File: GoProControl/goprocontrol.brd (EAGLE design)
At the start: 54.2 x 51.8 mm, 17 parts, among them Q1 IRLML6344

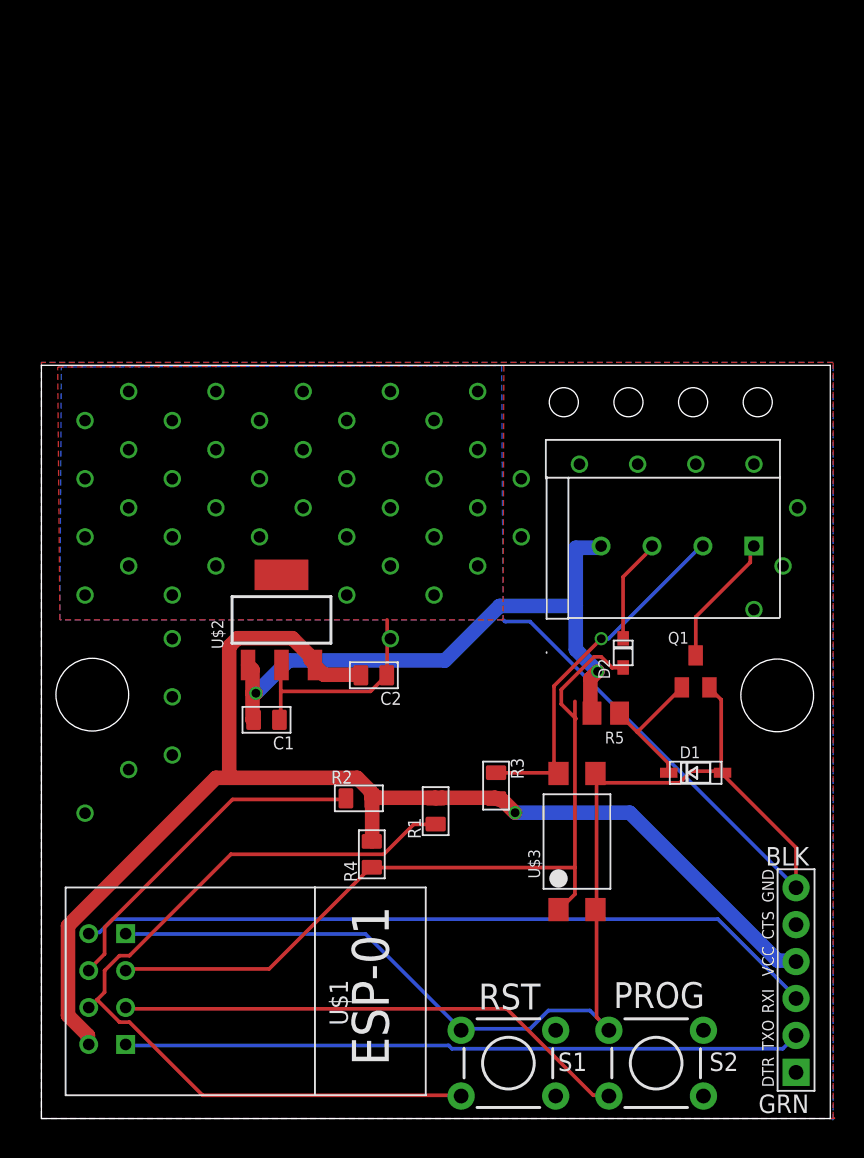
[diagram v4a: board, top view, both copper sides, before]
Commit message: v0.3
- heat sink vias are now 0.35mm and have no exposed copper
- 2x the number of heat sink vias
- improved labels
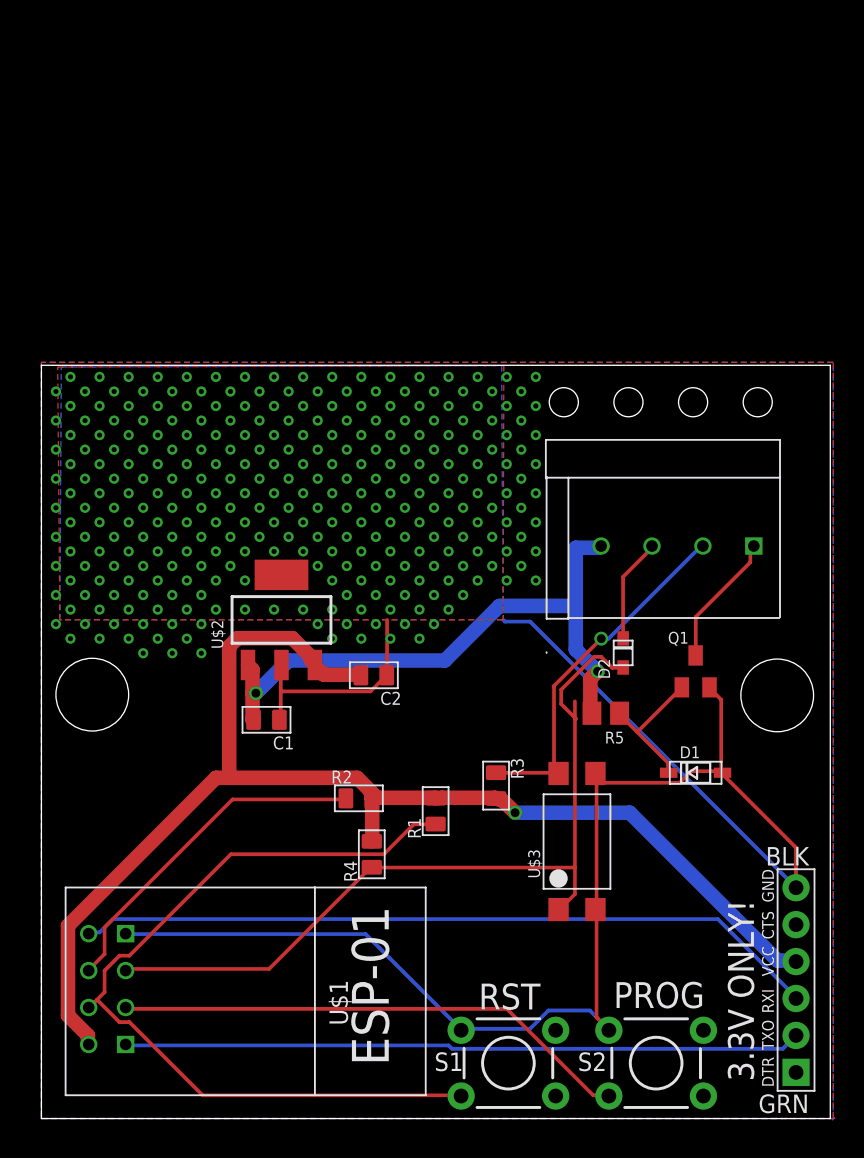
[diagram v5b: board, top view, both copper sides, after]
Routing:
- net GND: vias 53 -> 299
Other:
- board text added: "3.3V ONLY!"
- board text added: "GoProControl v0.3 http://synfin.net/goprocontrol"
- board text removed: "GoProControl v0.2 http://synfin.net/goprocontrol"

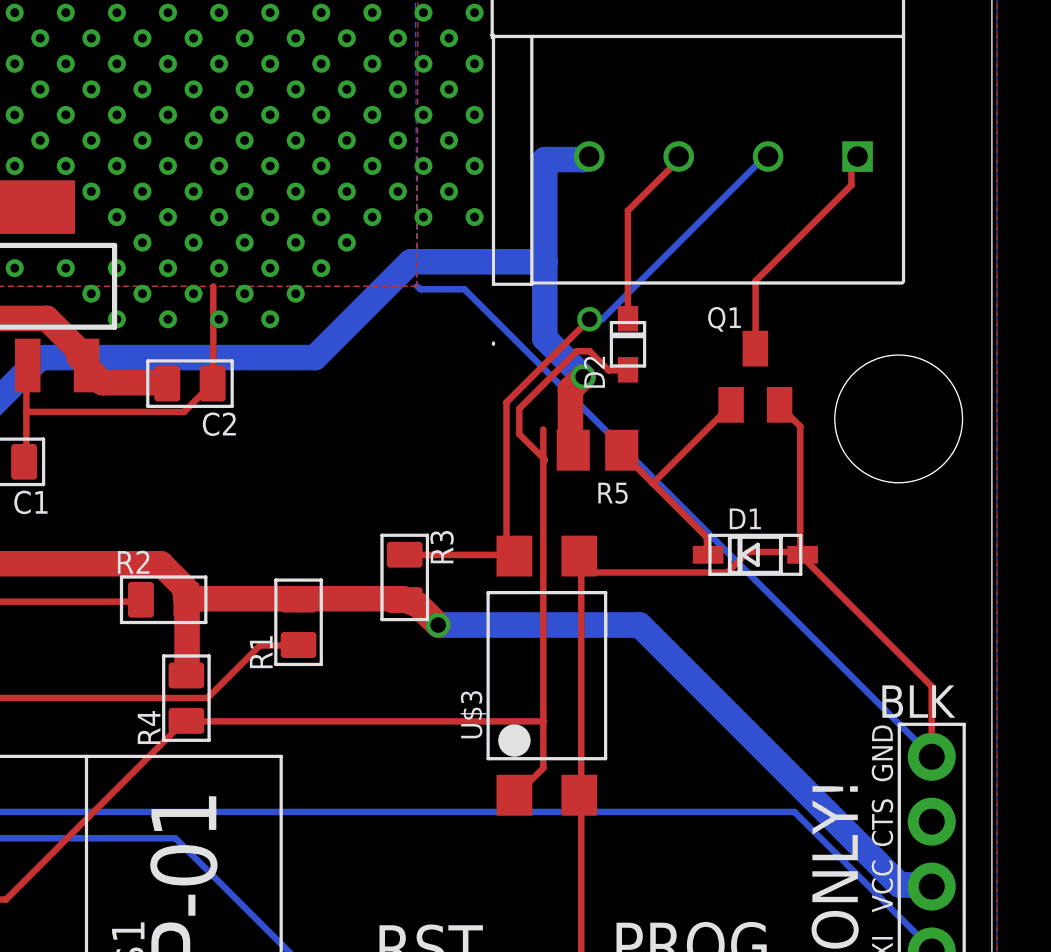
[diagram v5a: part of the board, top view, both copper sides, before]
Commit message: v0.4 fix diode pads
My old sod-323 and sod-123 pads always seemed a bit wrong/too small
these new pads are better.
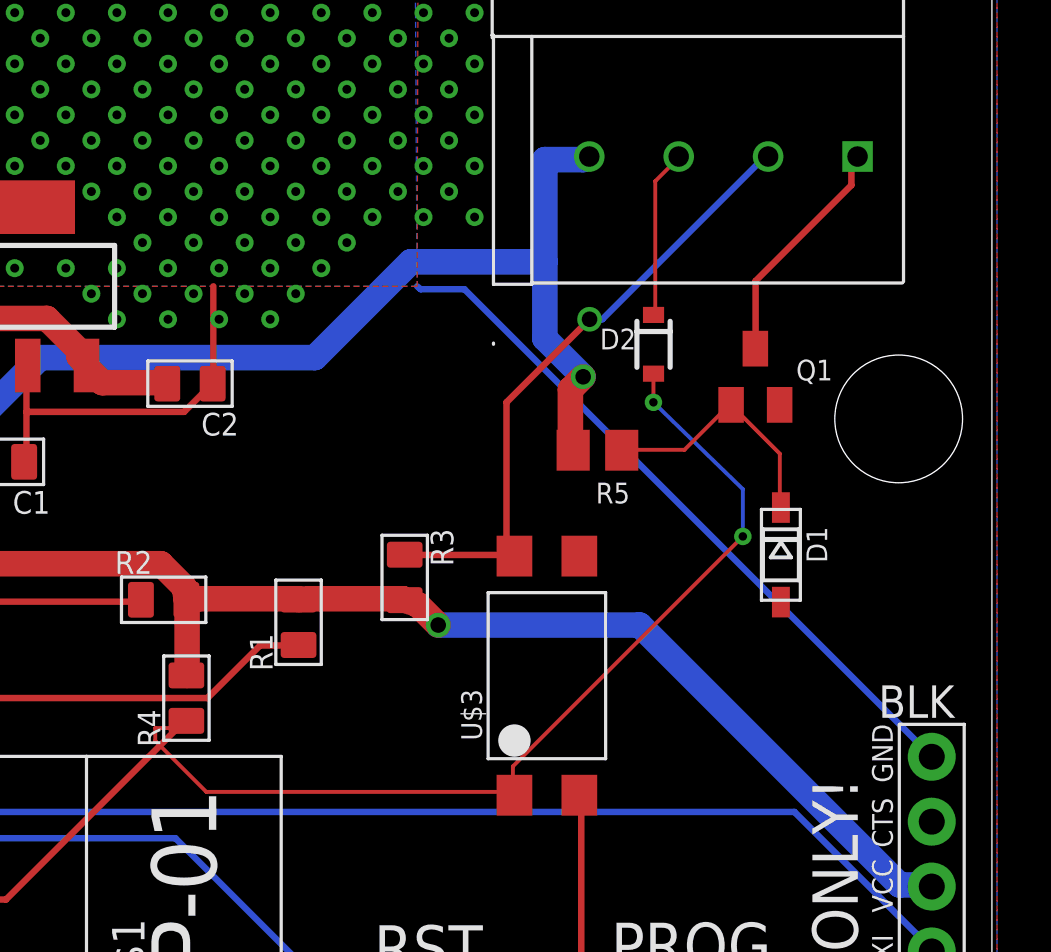
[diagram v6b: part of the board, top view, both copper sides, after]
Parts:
- D2: device synfinatic:SOD-323F -> synfinatic:SOD-323
- moved D1 1.00 mm to (46.0, 23.8), turned to 270 degrees
- moved D2 1.00 mm to (41.0, 32.0), turned to 270 degrees
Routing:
- net GND: track 124.3 -> 89.0 mm
- net GPIO2: track 56.7 -> 58.6 mm, vias 0 -> 2
- net INPUT: track 7.22 -> 6.61 mm
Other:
- board text added: "GoProControl v0.4 http://synfin.net/goprocontrol"
- board text removed: "GoProControl v0.3 http://synfin.net/goprocontrol"
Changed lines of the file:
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@@
 <grid distance="1" unitdist="mm" unit="mm" style="lines" multiple="1" display="no" altdistance="0.05" altunitdist="mm" altunit="mm"/>
 <layers>
-<layer number="1" name="Top" color="4" fill="1" visible="yes" active="yes"/>
-<layer number="16" name="Bottom" color="1" fill="1" visible="yes" active="yes"/>
+<layer number="1" name="Top" color="4" fill="1" visible="no" active="yes"/>
+<layer number="16" name="Bottom" color="1" fill="1" visible="no" active="yes"/>
 <layer number="17" name="Pads" color="2" fill="1" visible="yes" active="yes"/>
 <layer number="18" name="Vias" color="2" fill="1" visible="yes" active="yes"/>
@@
 <hole x="3.5" y="29.15" drill="5"/>
 <hole x="50.6" y="29.1" drill="5"/>
-<text x="48" y="16" size="1.016" layer="26" rot="MR0">GoProControl v0.3
+<text x="48" y="16" size="1.016" layer="26" rot="MR0">GoProControl v0.4
 http://synfin.net/goprocontrol</text>
 <text x="48" y="11.5" size="1.778" layer="26" rot="MR0">S/N:</text>
@@
 <attribute name="NAME" x="24.765" y="29.337" size="0.889" layer="25" font="vector" ratio="11" rot="R180"/>
 </element>
-<element name="D1" library="adafruit" package="SOD-123" value="10V Z" x="44.99" y="23.78" smashed="yes">
-<attribute name="NAME" x="43.89" y="24.78" size="0.8128" layer="25"/>
-</element>
-<element name="D2" library="synfinatic" package="SOD-323F" value="B5817WS" x="40.005" y="32.02" smashed="yes" rot="R90">
-<attribute name="NAME" x="39.105" y="30.22" size="0.8128" layer="25" font="vector" rot="R90"/>
+<element name="D1" library="adafruit" package="SOD-123" value="10V Z" x="45.99" y="23.78" smashed="yes" rot="R270">
+<attribute name="NAME" x="46.99" y="24.88" size="0.8128" layer="25" rot="R270"/>
+</element>
+<element name="D2" library="synfinatic" package="SOD-323" value="B5817WS" x="41.005" y="32.02" smashed="yes" rot="R270">
+<attribute name="NAME" x="38.905" y="31.82" size="0.8128" layer="25" font="vector"/>
 </element>
 <element name="JP1" library="SparkFun-Connectors" package="FTDI_DEVICE_SIDE" value="FTDI_DEVICE" x="51.895" y="9.525" rot="R90"/>
 <element name="Q1" library="synfinatic" package="SOT23" value="IRLML6344" x="44.99" y="30.75" smashed="yes">
-<attribute name="NAME" x="43.085" y="32.655" size="0.8128" layer="25"/>
+<attribute name="NAME" x="46.585" y="30.605" size="0.8128" layer="25"/>
 </element>
 <element name="R1" library="Seeed-OPL-Resistor" package="R0805" value="1K" x="27.11" y="21.14" smashed="yes" rot="R180">
@@
 <wire x1="16.4592" y1="29.3751" x2="22.6314" y2="29.3751" width="0.254" layer="1"/>
 <wire x1="23.6601" y1="30.4038" x2="23.749" y2="30.48" width="0.254" layer="1"/>
-<wire x1="46.7487" y1="28.8036" x2="46.7487" y2="23.8887" width="0.254" layer="1"/>
-<wire x1="45.9486" y1="29.6037" x2="46.7487" y2="28.8036" width="0.254" layer="1"/>
-<wire x1="46.7487" y1="23.8887" x2="46.84" y2="23.78" width="0.254" layer="1"/>
-<wire x1="45.9486" y1="29.6037" x2="45.94" y2="29.65" width="0.254" layer="1"/>
 <wire x1="38.1762" y1="6.9723" x2="38.1762" y2="14.2875" width="0.254" layer="1"/>
 <wire x1="38.9763" y1="6.1722" x2="38.1762" y2="6.9723" width="0.254" layer="1"/>
 <wire x1="38.1762" y1="14.2875" x2="38.1" y2="14.37" width="0.254" layer="1"/>
 <wire x1="38.9763" y1="6.1722" x2="39.0238" y2="6.0706" width="0.254" layer="1"/>
-<wire x1="38.1762" y1="14.4018" x2="38.1762" y2="23.6601" width="0.254" layer="1"/>
-<wire x1="38.1762" y1="23.6601" x2="38.1" y2="23.73" width="0.254" layer="1"/>
-<wire x1="38.1762" y1="14.4018" x2="38.1" y2="14.37" width="0.254" layer="1"/>
-<wire x1="44.6913" y1="23.8887" x2="46.6344" y2="23.8887" width="0.254" layer="1"/>
-<wire x1="43.8912" y1="23.0886" x2="44.6913" y2="23.8887" width="0.254" layer="1"/>
-<wire x1="38.2905" y1="23.0886" x2="43.8912" y2="23.0886" width="0.254" layer="1"/>
-<wire x1="46.6344" y1="23.8887" x2="46.84" y2="23.78" width="0.254" layer="1"/>
-<wire x1="38.2905" y1="23.0886" x2="38.1" y2="23.73" width="0.254" layer="1"/>
-<wire x1="51.8922" y1="18.6309" x2="51.8922" y2="15.8877" width="0.254" layer="1"/>
-<wire x1="46.863" y1="23.6601" x2="51.8922" y2="18.6309" width="0.254" layer="1"/>
-<wire x1="51.8922" y1="15.8877" x2="51.895" y2="15.875" width="0.254" layer="1"/>
-<wire x1="46.863" y1="23.6601" x2="46.84" y2="23.78" width="0.254" layer="1"/>
 <wire x1="33.6042" y1="34.1757" x2="31.8897" y2="34.1757" width="0.254" layer="16"/>
 <wire x1="51.8922" y1="15.8877" x2="33.6042" y2="34.1757" width="0.254" layer="16"/>
@@
 <contactref element="R5" pad="1"/>
 <contactref element="D1" pad="C"/>
-<wire x1="43.0911" y1="24.4602" x2="43.0911" y2="23.8887" width="0.254" layer="1"/>
-<wire x1="39.7764" y1="27.7749" x2="40.97655" y2="26.57475" width="0.254" layer="1"/>
-<wire x1="40.97655" y1="26.57475" x2="43.0911" y2="24.4602" width="0.254" layer="1"/>
-<wire x1="43.0911" y1="23.8887" x2="43.14" y2="23.78" width="0.254" layer="1"/>
-<wire x1="39.7764" y1="27.7749" x2="39.76" y2="27.875" width="0.254" layer="1"/>
-<wire x1="40.97655" y1="26.57475" x2="44.0055" y2="29.6037" width="0.254" layer="1"/>
-<wire x1="44.0055" y1="29.6037" x2="44.04" y2="29.65" width="0.254" layer="1"/>
+<wire x1="45.9486" y1="27.7368" x2="45.9486" y2="25.6794" width="0.1524" layer="1"/>
+<wire x1="44.0436" y1="29.6418" x2="45.9486" y2="27.7368" width="0.1524" layer="1"/>
+<wire x1="45.9486" y1="25.6794" x2="45.99" y2="25.63" width="0.1524" layer="1"/>
+<wire x1="44.0436" y1="29.6418" x2="44.04" y2="29.65" width="0.1524" layer="1"/>
+<wire x1="42.2148" y1="27.8892" x2="39.7764" y2="27.8892" width="0.1524" layer="1"/>
+<wire x1="43.9674" y1="29.6418" x2="42.2148" y2="27.8892" width="0.1524" layer="1"/>
+<wire x1="39.7764" y1="27.8892" x2="39.76" y2="27.875" width="0.1524" layer="1"/>
+<wire x1="43.9674" y1="29.6418" x2="44.04" y2="29.65" width="0.1524" layer="1"/>
 </signal>
 <signal name="GND_MAIN">
@@
 <contactref element="R4" pad="1"/>
 <contactref element="U$3" pad="1"/>
-<wire x1="36.6903" y1="15.4305" x2="36.6903" y2="17.2593" width="0.254" layer="1"/>
-<wire x1="36.6903" y1="17.2593" x2="36.6903" y2="27.5" width="0.254" layer="1"/>
-<wire x1="36.6903" y1="27.5" x2="36.6903" y2="28.6893" width="0.254" layer="1"/>
-<wire x1="35.6616" y1="14.4018" x2="36.6903" y2="15.4305" width="0.254" layer="1"/>
-<wire x1="35.6616" y1="14.4018" x2="35.56" y2="14.37" width="0.254" layer="1"/>
-<wire x1="36.6903" y1="17.2593" x2="22.7457" y2="17.2593" width="0.254" layer="1"/>
-<wire x1="22.7457" y1="17.2593" x2="22.72" y2="17.281" width="0.254" layer="1"/>
 <wire x1="15.6591" y1="10.287" x2="5.8293" y2="10.287" width="0.254" layer="1"/>
 <wire x1="22.6314" y1="17.2593" x2="15.6591" y2="10.287" width="0.254" layer="1"/>
 <wire x1="5.8293" y1="10.287" x2="5.7925" y2="10.175" width="0.254" layer="1"/>
 <wire x1="22.6314" y1="17.2593" x2="22.72" y2="17.281" width="0.254" layer="1"/>
-<wire x1="39.25" y1="31" x2="40" y2="31" width="0.254" layer="1"/>
-<wire x1="38.5" y1="31.75" x2="39.25" y2="31" width="0.254" layer="1"/>
-<wire x1="38" y1="31.75" x2="38.5" y2="31.75" width="0.254" layer="1"/>
-<wire x1="35.75" y1="29.5" x2="38" y2="31.75" width="0.254" layer="1"/>
-<wire x1="35.75" y1="28.5" x2="35.75" y2="29.5" width="0.254" layer="1"/>
-<wire x1="36.75" y1="27.5" x2="35.75" y2="28.5" width="0.254" layer="1"/>
-<wire x1="40" y1="31" x2="40.005" y2="31.02" width="0.254" layer="1"/>
-<wire x1="36.75" y1="27.5" x2="36.6903" y2="27.5" width="0.254" layer="1"/>
+<wire x1="41" y1="29.75" x2="41" y2="31" width="0.1524" layer="1"/>
+<wire x1="44.5" y1="26.35" x2="41" y2="29.75" width="0.1524" layer="16"/>
+<wire x1="44.5" y1="24.5" x2="44.5" y2="26.35" width="0.1524" layer="16"/>
+<wire x1="35.5" y1="15.5" x2="44.5" y2="24.5" width="0.1524" layer="1"/>
+<wire x1="35.5" y1="14.5" x2="35.5" y2="15.5" width="0.1524" layer="1"/>
+<wire x1="41" y1="31" x2="41.005" y2="30.87" width="0.1524" layer="1"/>
+<wire x1="23.5" y1="14.5" x2="35.5" y2="14.5" width="0.1524" layer="1"/>
+<wire x1="21.5" y1="16.5" x2="23.5" y2="14.5" width="0.1524" layer="1"/>
+<wire x1="21.5" y1="17" x2="21.5" y2="16.5" width="0.1524" layer="1"/>
+<wire x1="22.5" y1="17" x2="21.5" y2="17" width="0.1524" layer="1"/>
+<wire x1="35.5" y1="14.5" x2="35.56" y2="14.37" width="0.1524" layer="1"/>
+<wire x1="22.5" y1="17" x2="22.72" y2="17.281" width="0.1524" layer="1"/>
+<via x="41" y="29.75" extent="1-16" drill="0.3302"/>
+<via x="44.5" y="24.5" extent="1-16" drill="0.3302"/>
 </signal>
 <signal name="DTR">
@@
 <contactref element="D2" pad="C"/>
 <contactref element="U$4" pad="P$3"/>
-<wire x1="40" y1="37.25" x2="40" y2="33.25" width="0.254" layer="1"/>
-<wire x1="41.75" y1="39" x2="40" y2="37.25" width="0.254" layer="1"/>
-<wire x1="41.75" y1="39.25" x2="41.75" y2="39" width="0.254" layer="1"/>
-<wire x1="40" y1="33.25" x2="40.005" y2="33.02" width="0.254" layer="1"/>
-<wire x1="41.75" y1="39.25" x2="41.99" y2="39.37" width="0.254" layer="1"/>
+<wire x1="41.0718" y1="38.4048" x2="41.0718" y2="33.2232" width="0.1524" layer="1"/>
+<wire x1="41.9862" y1="39.3192" x2="41.0718" y2="38.4048" width="0.1524" layer="1"/>
+<wire x1="41.0718" y1="33.2232" x2="41.005" y2="33.17" width="0.1524" layer="1"/>
+<wire x1="41.9862" y1="39.3192" x2="41.99" y2="39.37" width="0.1524" layer="1"/>
 </signal>
 <signal name="OUTPUT">
